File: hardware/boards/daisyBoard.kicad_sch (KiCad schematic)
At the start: 96 parts, among them IC1 TL072, IC2 TL072, IC3 TL072, IC4 TL072, J1 LEFT Pin ROW, J10 AudioJack_OUT_2, J11 AudioJack_OUT_2, J12 Micro_SD_Card, J13 LEFT Pin ROW Daisy, J14 RIGHT Pin ROW DAISY, J15 Daisy Pin Breakout LEFT, J16 Daisy PIN Breakout RIGHT, J2 RIGHT Pin Row, J3 ESP32 Pin Breakout RIGHT, J4 ESP32 Pin Breakout LEFT, J5 Micro_SD_Card, J6 AudioJack3, J7 AudioJack3, J8 AudioJack_IN_1, J9 AudioJack_IN_2, U1 MCP6002-xSN, U2 MCP6002-xSN, U3 MCP6002-xSN

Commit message: Added compatible components
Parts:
- removed C18: 10uF, Capacitor_SMD:C_1206_3216Metric, symbol Device:C
- removed FB2, FB3: 60R @ 100MHz, Inductor_SMD:L_0805_2012Metric, symbol Device:FerriteBead
- removed J12, J5: Micro_SD_Card, Connector_Card:microSD_HC_Molex_104031-0811, symbol Connector:Micro_SD_Card
- added 100nF: C26, Capacitor_SMD:C_1206_3216Metric, symbol Device:C
- added C24: 10uF, Capacitor_SMD:C_1206_3216Metric, symbol Device:C
- added C25: 100nF, Capacitor_SMD:C_1206_3216Metric, symbol Device:C
- added Card1, Card2: TF-01A, lcsc_footprints:C91145_TF-SMD_TF-01A, symbol lcsc_imported:TF-01A
- C14: value 0.1uF -> 10uF
- R13, R14, R15, R16, R17, R25, R26, R27: value 10K -> 47K
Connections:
- net GNDA is gone; now on net GND: C1.2, C10.2, C13.2, C15.2, C16.2, C17.2, C19.2, C20.2, C3.1, C4.2, C6.1, C7.2, IC1.4 (V-), IC2.4 (V-), IC3.4 (V-), IC4.4 (V-), J10.S, J11.S, J13.1 (Pin_1), J14.1 (Pin_1), J15.20 (Pin_20), J16.20 (Pin_20), J6.S, J7.S, J8.S, J9.S, R12.2, R19.2, R20.2, R23.1, R8.2, TP10.1, TP12.1, TP15.1, TP17.1, TP19.1, TP9.1, U1.4 (V-), U2.4 (V-), U3.4 (V-)
- net GNDD is gone; now on net GND: C14.1, C21.2, C22.2, C23.2, J1.2 (Pin_2), J2.14 (Pin_14), J3.2 (Pin_2), J4.14 (Pin_14)
- net +3.3VD: now also C14.2, 100nF.2, Card1.4 (VDD)
- net ESP-3.3V: now also C24.2, C25.2, Card2.4 (VDD); no longer C14.2
- net GND: now also 100nF.1, C24.1, C25.1, Card1.10 (GND), Card1.11 (GND), Card1.12 (GND), Card1.13 (GND), Card1.6 (VSS), Card2.10 (GND), Card2.11 (GND), Card2.12 (GND), Card2.13 (GND), Card2.6 (VSS)
- net SD_CLK_DAISY: now also Card1.5 (CLK(SCLK))
- net SD_CMD_DAISY: now also R17.2, Card1.3 (CMD(DI)); no longer R15.2
- net SD_CS: now also R26.2, Card2.2 (CDDAT3(CS)); no longer R25.2
- net SD_DAT_0_DAISY: now also R13.2, Card1.7 (DAT0(D0)); no longer R16.2
- net SD_DAT_1_DAISY: now also R14.2, Card1.8 (DAT1(RSV)); no longer R17.2
- net SD_DAT_2_DAISY: now also R15.2, Card1.1 (DAT2(RSV)); no longer R13.2
- net SD_DAT_3_DAISY: now also R16.2, Card1.2 (CDDAT3(CS)); no longer R14.2
- net SD_MISO: now also R25.2, Card2.7 (DAT0(D0)); no longer R27.2
- net SD_MOSI: now also R27.2, Card2.3 (CMD(DI)); no longer R26.2
- net SD_SCK: now also Card2.5 (CLK(SCLK))
- no-connect marks 23 -> 25
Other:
- note removed: "Decoup Caps close to VDD input"

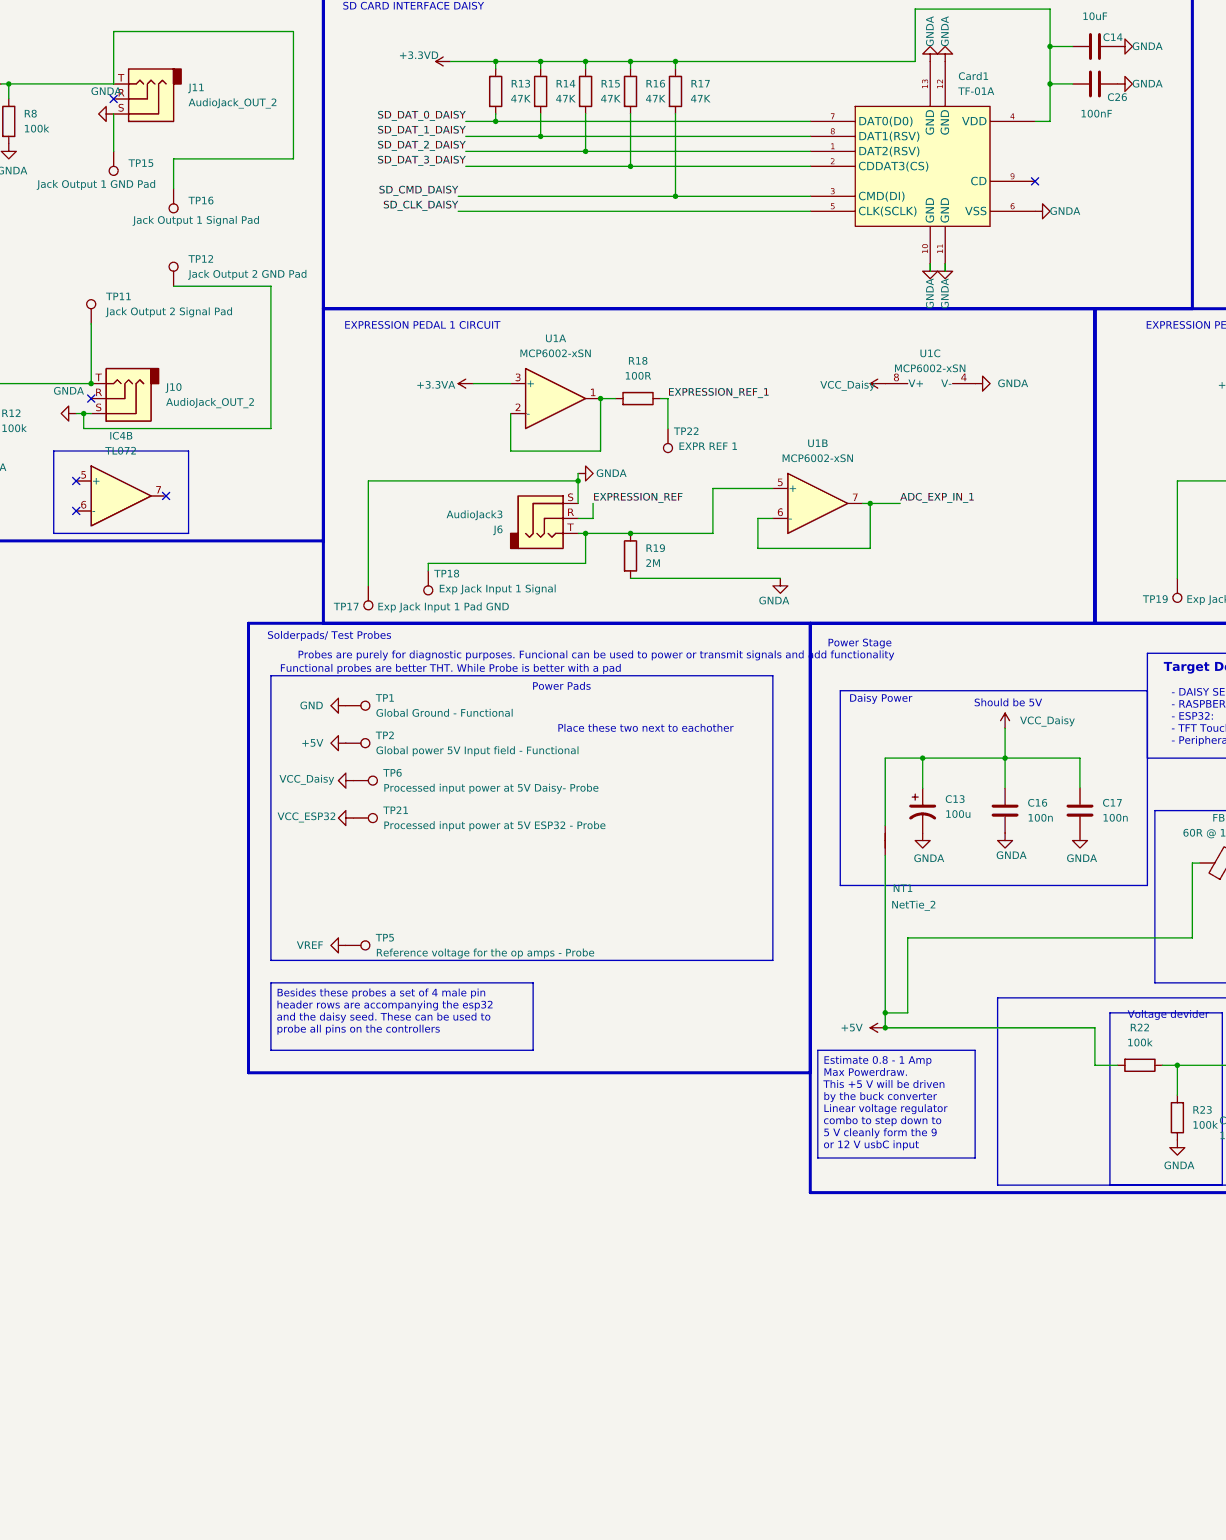
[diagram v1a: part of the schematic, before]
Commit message: updated design and added start for indicator leds on design
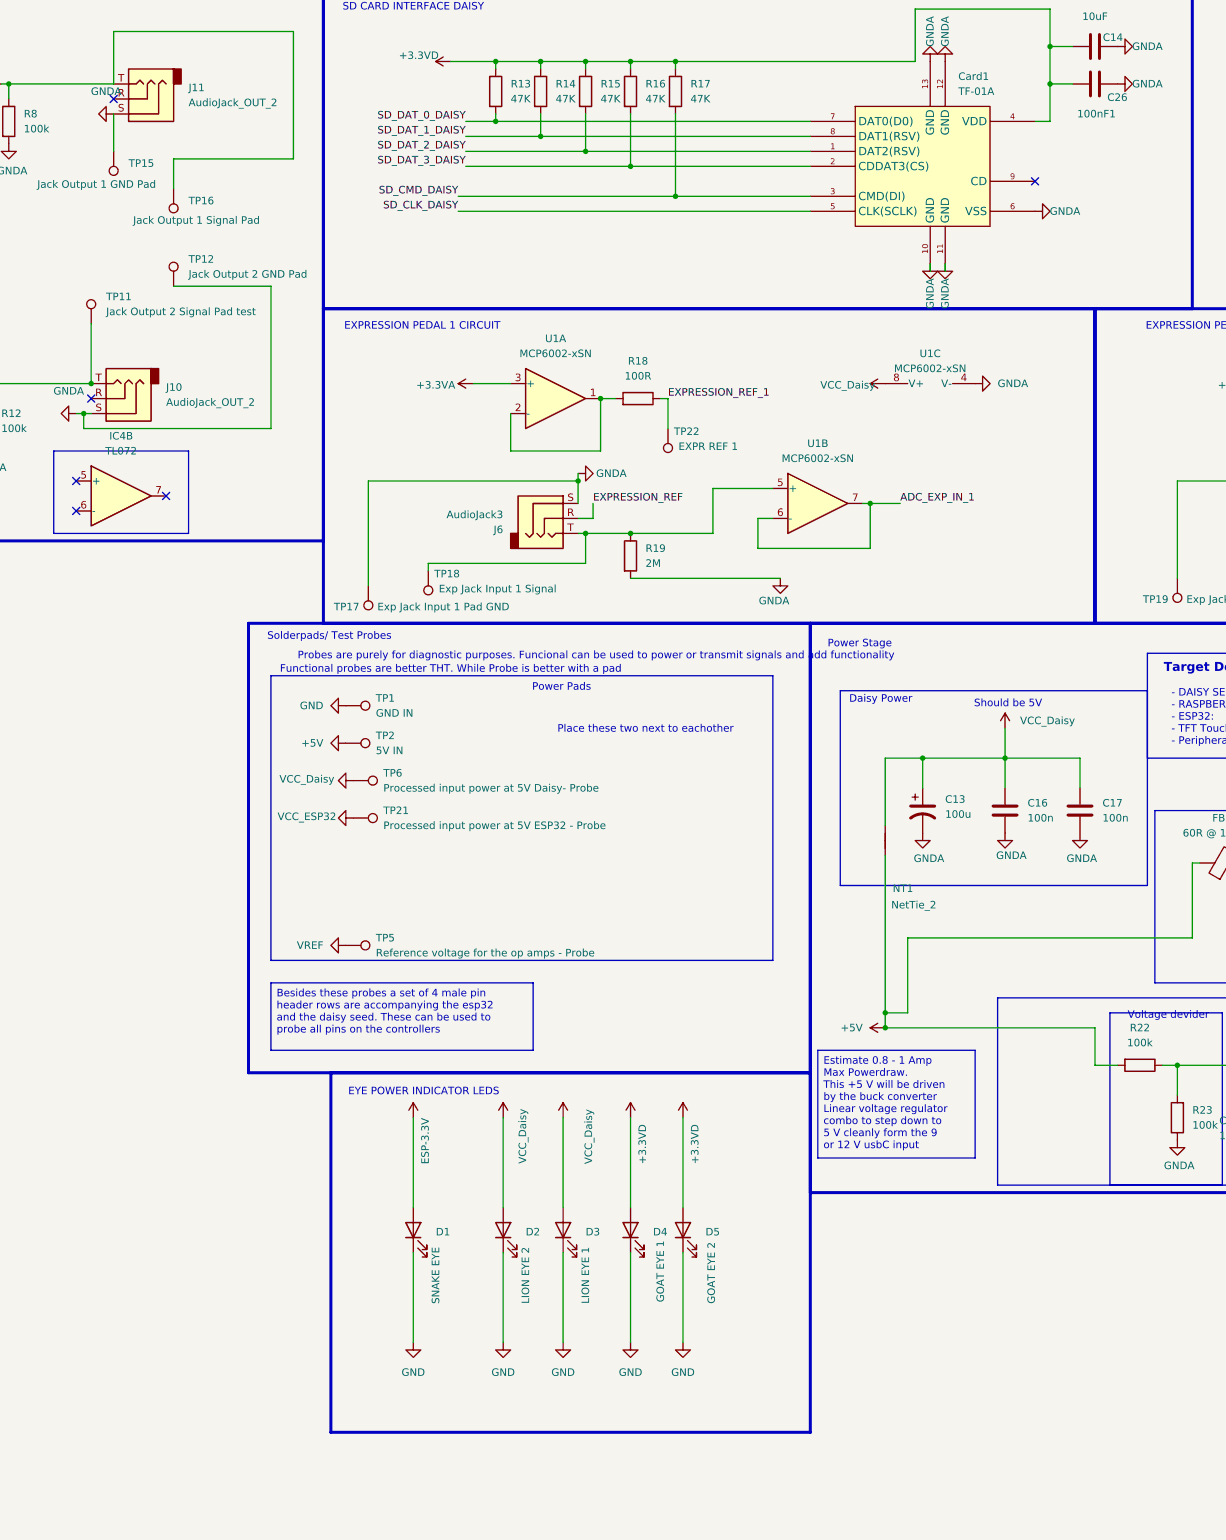
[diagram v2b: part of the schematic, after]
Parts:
- added D1: SNAKE EYE, LED_SMD:LED_0201_0603Metric, symbol Device:LED
- added D2: LION EYE 2, LED_SMD:LED_0201_0603Metric, symbol Device:LED
- added D3: LION EYE 1, LED_SMD:LED_0201_0603Metric, symbol Device:LED
- added D4: GOAT EYE 1, LED_SMD:LED_0201_0603Metric, symbol Device:LED
- added D5: GOAT EYE 2, LED_SMD:LED_0201_0603Metric, symbol Device:LED
- TP1: value Global Ground - Functional -> GND IN
- TP11: value Jack Output 2 Signal Pad -> Jack Output 2 Signal Pad test
- TP2: value Global power 5V Input field - Functional -> 5V IN
- renumbered 100nF to 100nF1
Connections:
- net +3.3VD: now also D4.2 (A), D5.2 (A)
- net ESP-3.3V: now also D1.2 (A)
- net GND: now also D1.1 (K), D2.1 (K), D3.1 (K), D4.1 (K), D5.1 (K)
- net VCC_Daisy: now also D2.2 (A), D3.2 (A)
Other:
- note added: "EYE POWER INDICATOR LEDS"

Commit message: removed grbrs and updated corner design pcb and still need to add led resistors
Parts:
- D1: value SNAKE EYE -> SNAKE EYE - GREEN
- D2: value LION EYE 2 -> LION EYE 2 - YELLOW
- D3: value LION EYE 1 -> LION EYE 1 - YELLOW
- D4: value GOAT EYE 1 -> GOAT EYE 1 - RED
- D5: value GOAT EYE 2 -> GOAT EYE 2 - RED
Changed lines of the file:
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@@
 			)
 		)
-		(property "Value" "LION EYE 2"
+		(property "Value" "LION EYE 2 - YELLOW"
 			(at 326.39 237.8074 0)
 			(show_name no)
@@
 			)
 		)
-		(property "Value" "SNAKE EYE"
+		(property "Value" "SNAKE EYE - GREEN"
 			(at 311.15 237.8074 0)
 			(show_name no)
@@
 			)
 		)
-		(property "Value" "LION EYE 1"
+		(property "Value" "LION EYE 1 - YELLOW"
 			(at 336.55 237.8074 0)
 			(show_name no)
@@
 			)
 		)
-		(property "Value" "GOAT EYE 1"
+		(property "Value" "GOAT EYE 1 - RED"
 			(at 349.25 236.728 0)
 			(show_name no)
@@
 			)
 		)
-		(property "Value" "GOAT EYE 2"
+		(property "Value" "GOAT EYE 2 - RED"
 			(at 357.886 236.982 0)
 			(show_name no)

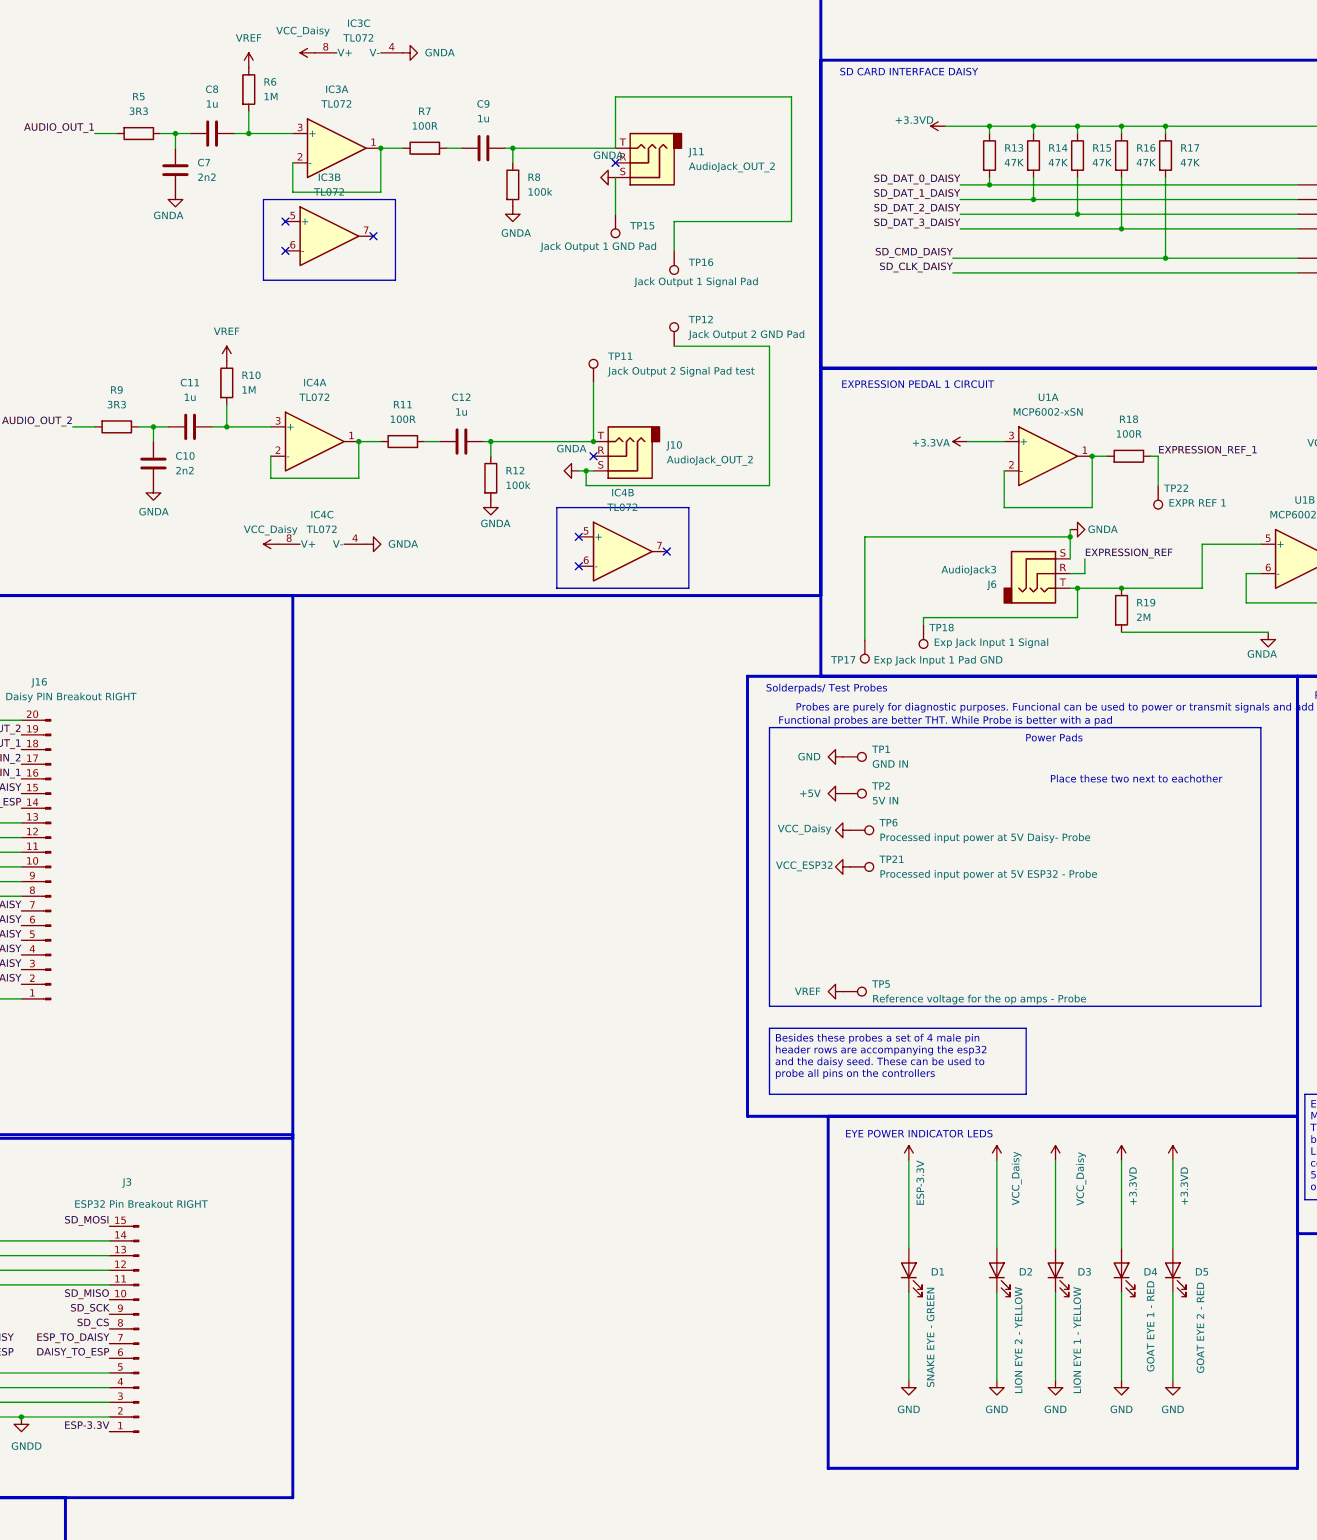
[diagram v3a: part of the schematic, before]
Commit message: added led values
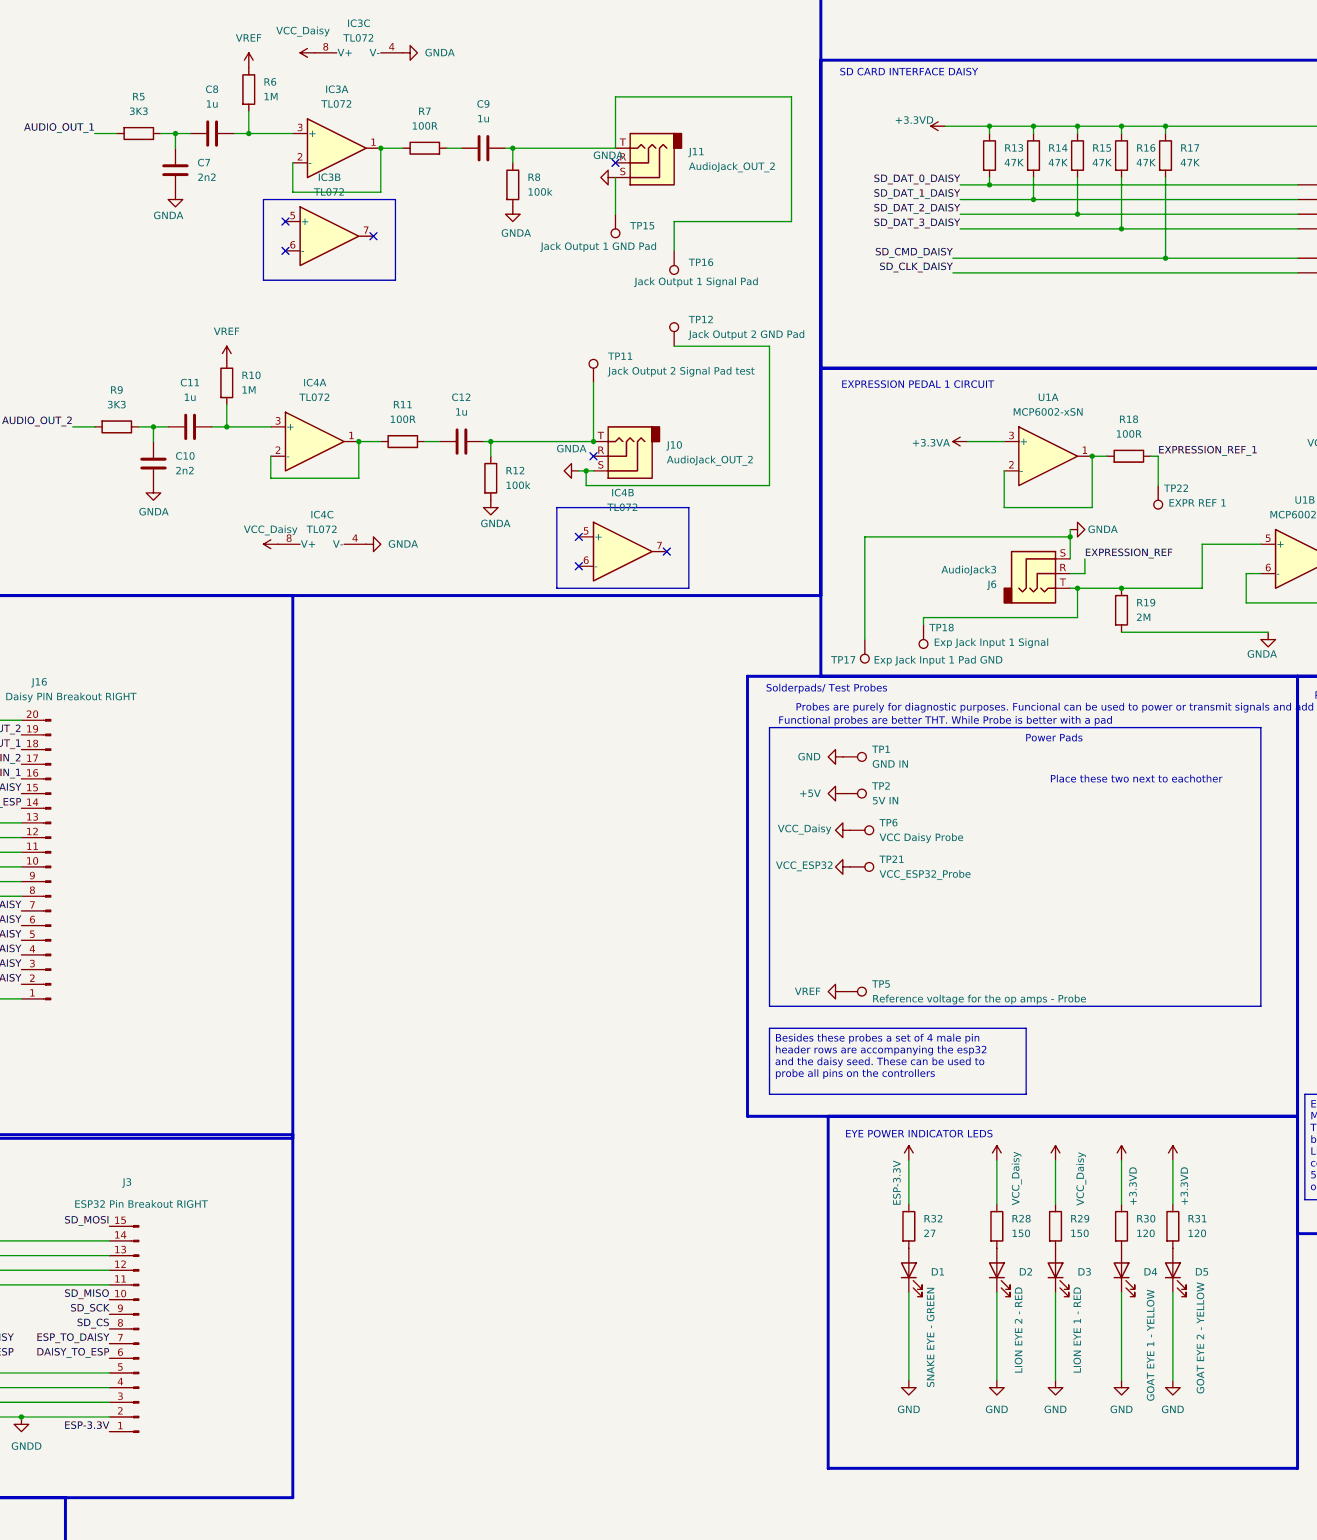
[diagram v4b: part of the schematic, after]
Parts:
- added R28, R29: 150, Resistor_SMD:R_0805_2012Metric, symbol Device:R
- added R30, R31: 120, Resistor_SMD:R_0805_2012Metric, symbol Device:R
- added R32: 27, Resistor_SMD:R_0805_2012Metric, symbol Device:R
- D2: value LION EYE 2 - YELLOW -> LION EYE 2 - RED
- D3: value LION EYE 1 - YELLOW -> LION EYE 1 - RED
- D4: value GOAT EYE 1 - RED -> GOAT EYE 1 - YELLOW
- D5: value GOAT EYE 2 - RED -> GOAT EYE 2 - YELLOW
- R5, R9: value 3R3 -> 3K3
- TP1, TP10, TP11, TP12, TP15, TP16, TP17, TP18, TP19, TP2, TP20, TP22, TP23, TP7, TP8, TP9: now left out of the parts list
- TP21: value Processed input power at 5V ESP32 - Probe -> VCC_ESP32_Probe
- TP6: value Processed input power at 5V Daisy- Probe -> VCC Daisy Probe
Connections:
- net +3.3VD: now also R30.1, R31.1; no longer D4.2 (A), D5.2 (A)
- net ESP-3.3V: now also R32.1; no longer D1.2 (A)
- net VCC_Daisy: now also R28.1, R29.1; no longer D2.2 (A), D3.2 (A)
- new net: D2.2 (A), R28.2
- new net: D1.2 (A), R32.2
- new net: D3.2 (A), R29.2
- new net: D4.2 (A), R30.2
- new net: D5.2 (A), R31.2

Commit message: Applied review and updated ground plane and power plane design
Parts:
- added C18, C26, C27, C28, C29, C30, C31: 100nF, symbol Device:C
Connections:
- net +5V: now also C31.2
- net GND: now also C18.1, C26.1, C27.1, C28.1, C29.1, C30.1, C31.1
- net VCC_Daisy: now also C18.2, C26.2, C27.2, C28.2, C29.2, C30.2
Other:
- moved on the sheet: IC2C, IC4C, U3C

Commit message: added larger ferrite bead in components 600ohm @ 100Mhz
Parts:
- FB1: value 60R @ 100MHz -> 600 Ω @ 100 MHz
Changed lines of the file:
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@@
 			)
 		)
-		(property "Value" "60R @ 100MHz"
+		(property "Value" "600 Ω @ 100 MHz"
 			(at 444.4492 167.64 90)
 			(show_name no)
